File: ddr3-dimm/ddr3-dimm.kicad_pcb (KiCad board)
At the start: 2 copper layers, 133.3 x 30.5 mm, 1 part, among them CN1 DDR3

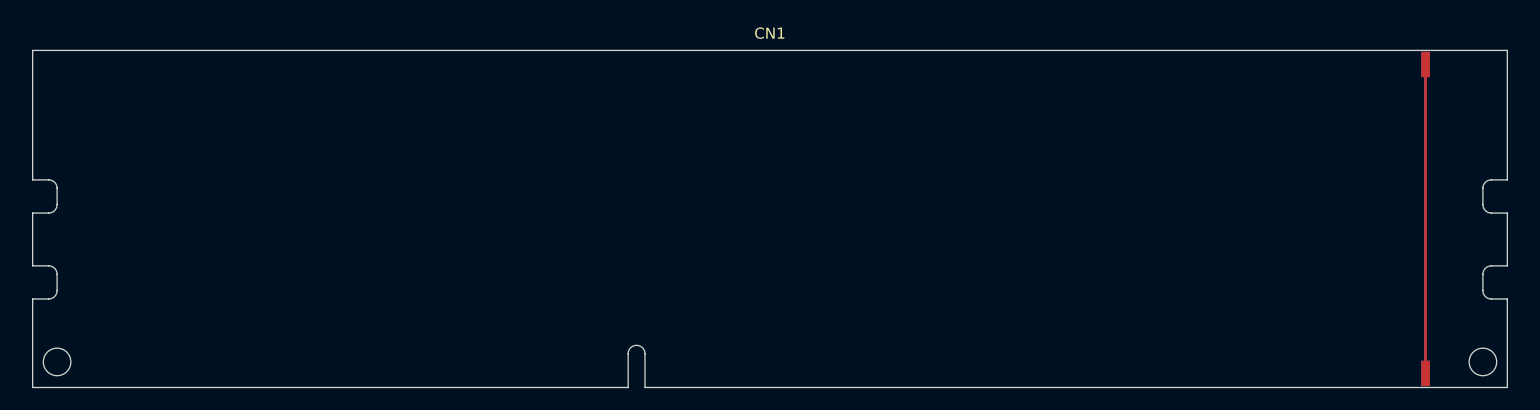
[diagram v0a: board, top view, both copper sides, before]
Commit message: ddr3-dimm: adjust the dimentions to manual measurement
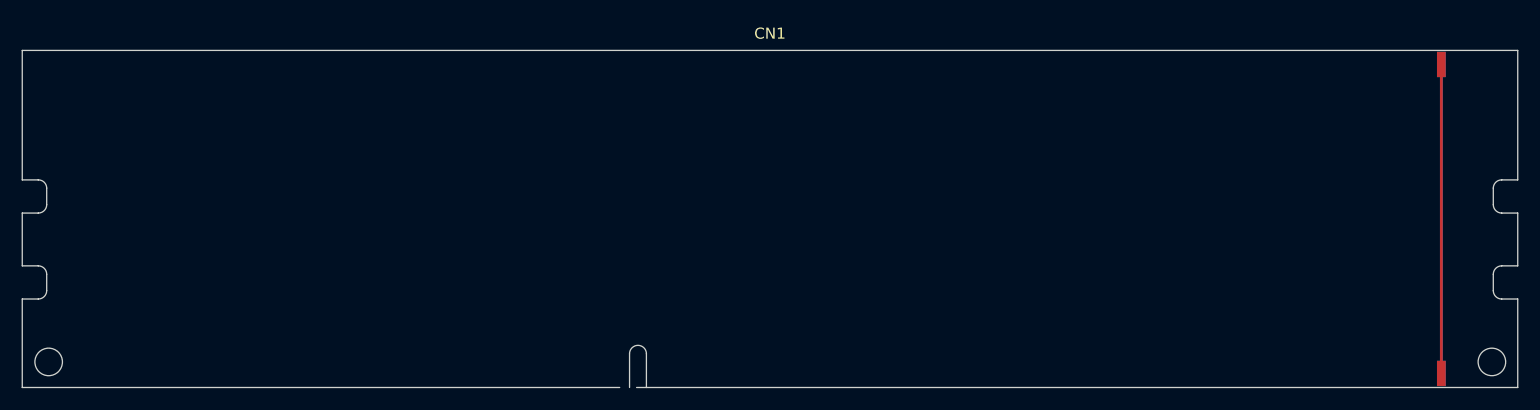
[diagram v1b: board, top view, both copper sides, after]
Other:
- board size 133.3 x 30.5 mm -> 135.2 x 30.5 mm
